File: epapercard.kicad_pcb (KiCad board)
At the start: 2 copper layers, 88.9 x 50.8 mm, 44 parts, among them P1 PROG, P2 A120699CT, Q1 2N7002KW, Q2 BSS84W, Q3 AP2305, Q4 BSS84W, Q5 2N7002KW, Q6 2N7002KW, Q7 2N7002KW, SW1 SW_PUSH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

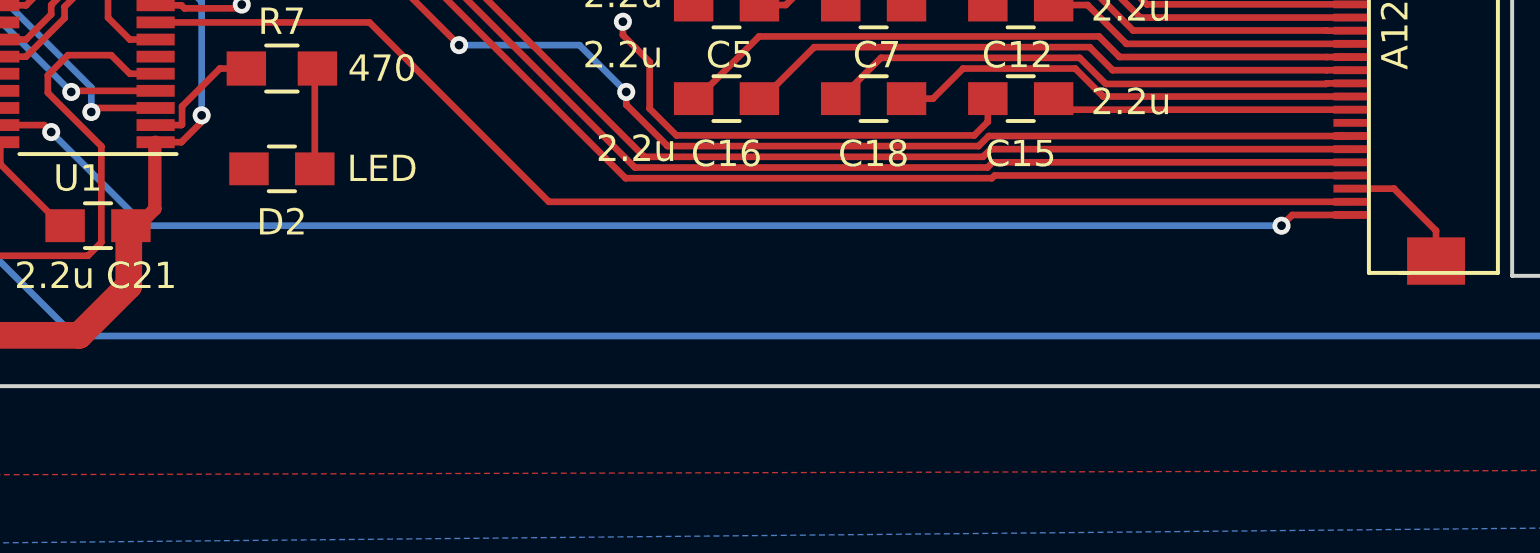
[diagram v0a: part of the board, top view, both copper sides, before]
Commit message: Updated silk
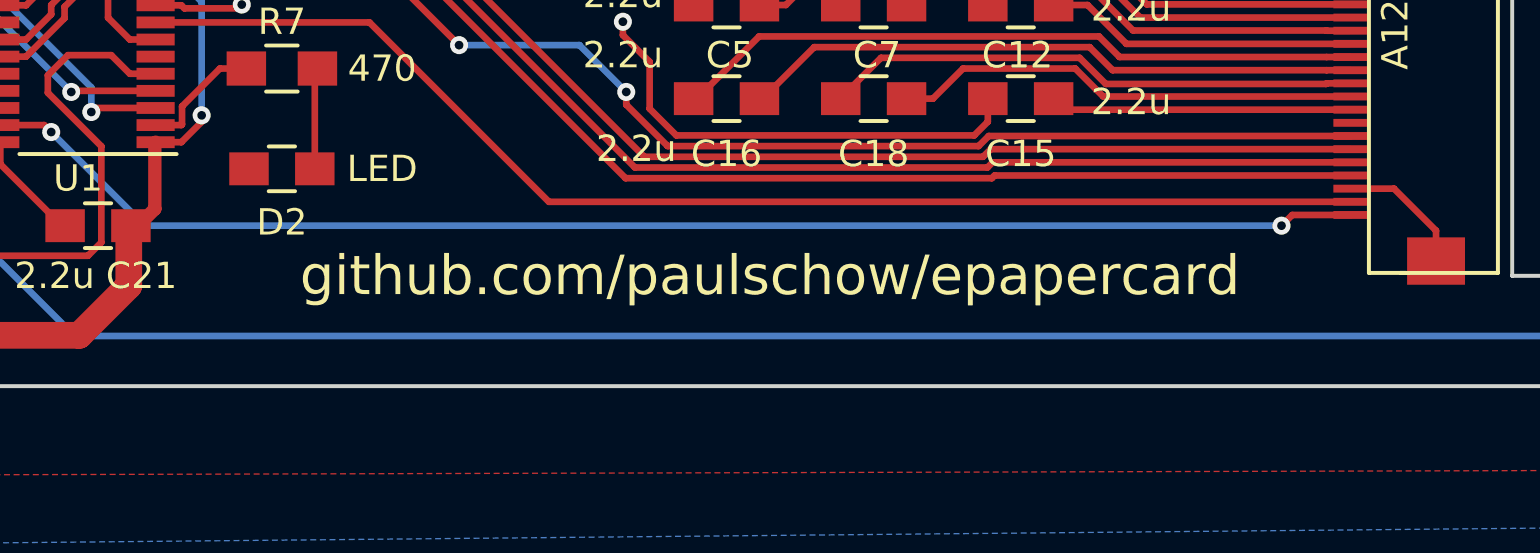
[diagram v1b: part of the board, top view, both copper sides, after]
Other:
- board text added: "github.com/paulschow/epapercard"
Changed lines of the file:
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@@
     (area 8.204287 22.759999 124.714001 86.868001)
     (thickness 1.6)
-    (drawings 29)
+    (drawings 30)
     (tracks 452)
     (zones 0)
@@
       (xy 0.317705 4.183579)) (layer B.SilkS) (width 0.01))
   )
+  (gr_text github.com/paulschow/epapercard (at 75.946 76.454) (layer F.SilkS)
+    (effects (font (size 1.5 1.5) (thickness 0.3)))
+  )
   (gr_text "Open Source\nHardware" (at 40.64 75.438) (layer B.SilkS)
     (effects (font (size 1.5 1.5) (thickness 0.3)) (justify mirror))
@@
     (effects (font (size 1.016 1.016) (thickness 0.1524)))
   )
-  (gr_text paulschow@gmail.com (at 88.138 40.386) (layer B.SilkS)
-    (effects (font (size 2.54 2.54) (thickness 0.3)) (justify mirror))
+  (gr_text paulschow@gmail.com (at 64.516 33.02) (layer B.SilkS)
+    (effects (font (size 2.54 2.54) (thickness 0.381)) (justify mirror))
   )
   (gr_text paulschow.com (at 94.996 36.322) (layer B.SilkS)
-    (effects (font (size 2.54 2.54) (thickness 0.3)) (justify mirror))
+    (effects (font (size 2.54 2.54) (thickness 0.381)) (justify mirror))
   )
   (gr_text "Paul Schow" (at 98.298 33.02) (layer B.SilkS)
-    (effects (font (size 2.54 2.54) (thickness 0.3)) (justify mirror))
+    (effects (font (size 2.54 2.54) (thickness 0.381)) (justify mirror))
   )
   (gr_text "CUT OUT" (at 105.41 63.754 90) (layer Edge.Cuts)

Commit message: Adjusting footprints
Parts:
- removed G***: LOGO, footprint:oshlogo
- P1: value PROG -> CONN_01X06
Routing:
- net BUSY: track 48.2 -> 17.8 mm
- net +3.3VP: track 74.4 -> 58.1 mm
- net GND: track 58.1 -> 42.4 mm, vias 3 -> 2
- net /RESET: track 48.3 -> 34.6 mm
- net SPI_MISO: track 57.7 -> 44.0 mm
- net SPI_MOSI: track 57.7 -> 44.1 mm
- net SPI_CLK: track 55.4 -> 41.9 mm
- net Net-(C15-Pad1): track 11.4 -> 0.59 mm
- net /VDL: track 35.7 -> 25.3 mm
- net Net-(C18-Pad1): track 17.8 -> 8.39 mm
- net Net-(C18-Pad2): track 20.4 -> 11.1 mm
- net Net-(C16-Pad1): track 23.6 -> 14.6 mm
- net Net-(C16-Pad2): track 26.3 -> 17.5 mm
- net Net-(C12-Pad1): track 11.9 -> 3.38 mm
- net Net-(C12-Pad2): track 15.5 -> 7.23 mm
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
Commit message: Basically starting over
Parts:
- C2: value 100n -> 0.1u
- Q3: value AP2305 -> BSS84W
- U1: footprint Housings_SSOP:TSSOP-20_4.4x6.5mm_Pitch0.65mm -> footprint:TSSOP-20_4.4x6.5mm_Pitch0.65mm
- moved Q4 94.4 mm to (41.3, 112.6), turned to 0 degrees
- moved R5 67.3 mm to (64.1, 112.5), turned to 0 degrees
- moved Q7 66.2 mm to (50.7, 93.8), turned to 0 degrees
- moved C4 65.8 mm to (65.2, 93.9)
- moved R3 63.5 mm to (78.4, 100.1), turned to 0 degrees
- moved C14 60.3 mm to (51.9, 115.7), turned to 0 degrees
- moved C9 59.3 mm to (47.0, 113.5), turned to 0 degrees
- moved R1 58.9 mm to (75.3, 106.3), turned to 0 degrees
- moved C11 57.5 mm to (60.3, 106.3), turned to 0 degrees
- moved D1 57.1 mm to (41.6, 107.9), turned to 0 degrees
- moved R2 55.8 mm to (69.3, 112.5), turned to 0 degrees
- moved R6 55.1 mm to (49.1, 107.3), turned to 0 degrees
- moved C17 54.5 mm to (79.3, 112.5), turned to 0 degrees
- moved Q5 52.1 mm to (42.3, 103.2), turned to 0 degrees
- moved R4 51.2 mm to (85.1, 93.9), turned to 0 degrees
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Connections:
- Q2 pad 2: Net-(C1-Pad2) -> +3V3
- Q2 pad 3: +3V3 -> Net-(C1-Pad2)
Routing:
- net +3V3: track 233.9 -> 93.9 mm, vias 4 -> 0
- net BORDER_CONTROL: track 109.9 -> 0.04 mm, vias 2 -> 0
- net /VGL: track 58.1 -> 0.00 mm
- net +3.3VP: track 58.1 -> 0.00 mm
- net /EPD_CS: track 50.3 -> 0.00 mm, vias 1 -> 0
- net SPI_MOSI: track 44.1 -> 0.00 mm
- net SPI_MISO: track 44.0 -> 0.00 mm
- net SPI_CLK: track 41.9 -> 0.00 mm
- net GND: track 42.4 -> 4.26 mm, vias 2 -> 0
- net /VDH: track 34.7 -> 0.00 mm
- net /RESET: track 34.6 -> 0.00 mm, vias 2 -> 0
- net /VGH: track 32.5 -> 0.00 mm
- net /VCOM: track 31.4 -> 0.00 mm, vias 2 -> 0
- net DISCHARGE: track 26.9 -> 0.00 mm, vias 3 -> 0
- net /VDL: track 25.3 -> 0.00 mm
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- removed copper zone on B.Cu, net GND
- removed copper zone on F.Cu, net GND
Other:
- outline, holes or cut-outs redrawn

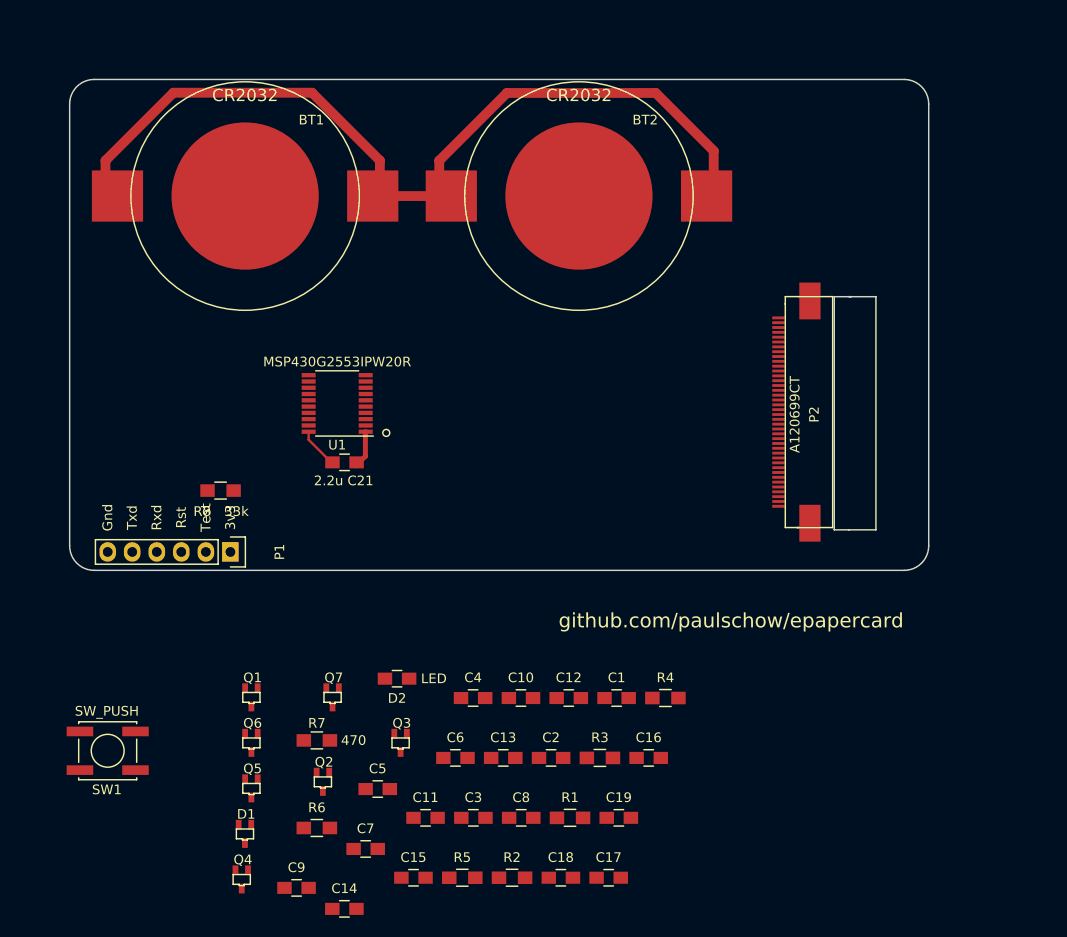
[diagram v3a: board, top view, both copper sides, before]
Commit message: Routed caps
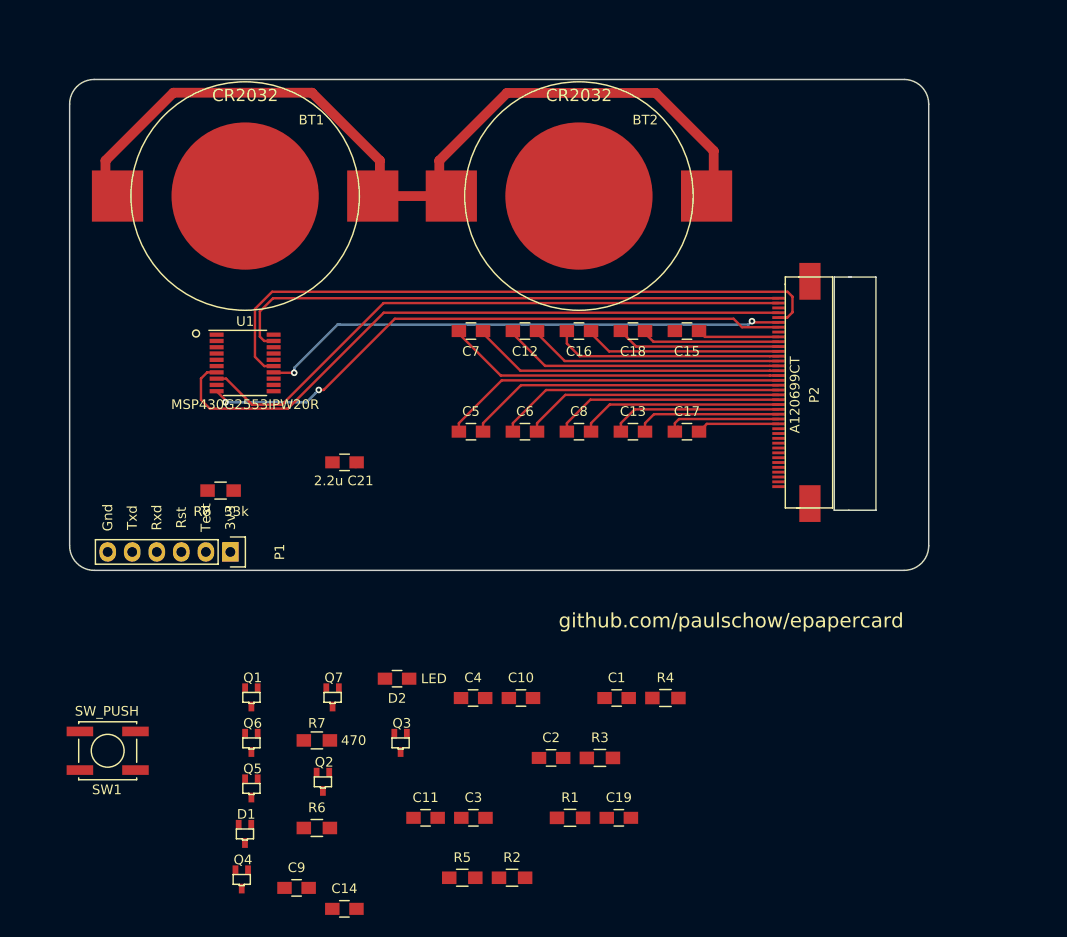
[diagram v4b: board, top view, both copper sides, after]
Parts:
- moved C15 63.3 mm to (87.4, 55.9), turned to 180 degrees
- moved C18 57.1 mm to (81.8, 55.9), turned to 180 degrees
- moved C7 54.7 mm to (65.0, 55.9), turned to 180 degrees
- moved C17 46.9 mm to (87.4, 66.3)
- moved C16 44.8 mm to (76.2, 55.9), turned to 180 degrees
- moved C8 40.4 mm to (76.2, 66.3)
- moved C12 38.2 mm to (70.6, 55.9), turned to 180 degrees
- moved C5 38.2 mm to (65.0, 66.3)
- moved C13 36.3 mm to (81.8, 66.3)
- moved C6 34.5 mm to (70.6, 66.3)
- moved U1 10.4 mm to (41.7, 59.2), turned to 0 degrees
- moved P2 2.03 mm to (101.9, 62.5)
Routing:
- net SPI_CLK: track 0.00 -> 68.3 mm
- net SPI_MOSI: track 0.00 -> 67.1 mm
- net BUSY: track 0.00 -> 63.6 mm
- net /RESET: track 0.00 -> 62.7 mm, vias 0 -> 2
- net /EPD_CS: track 0.00 -> 58.5 mm
- net SPI_MISO: track 0.00 -> 54.8 mm, vias 0 -> 2
- net Net-(C5-Pad1): track 0.00 -> 35.8 mm
- net Net-(C7-Pad2): track 0.00 -> 35.1 mm
- net Net-(C5-Pad2): track 0.00 -> 33.1 mm
- net Net-(C7-Pad1): track 0.00 -> 32.4 mm
- net Net-(C6-Pad1): track 0.00 -> 29.8 mm
- net Net-(C12-Pad2): track 0.00 -> 29.1 mm
- net Net-(C6-Pad2): track 0.00 -> 27.1 mm
- net Net-(C12-Pad1): track 0.00 -> 26.4 mm
- net Net-(C8-Pad1): track 0.00 -> 23.9 mm
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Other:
- outline, holes or cut-outs redrawn

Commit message: Placed all components
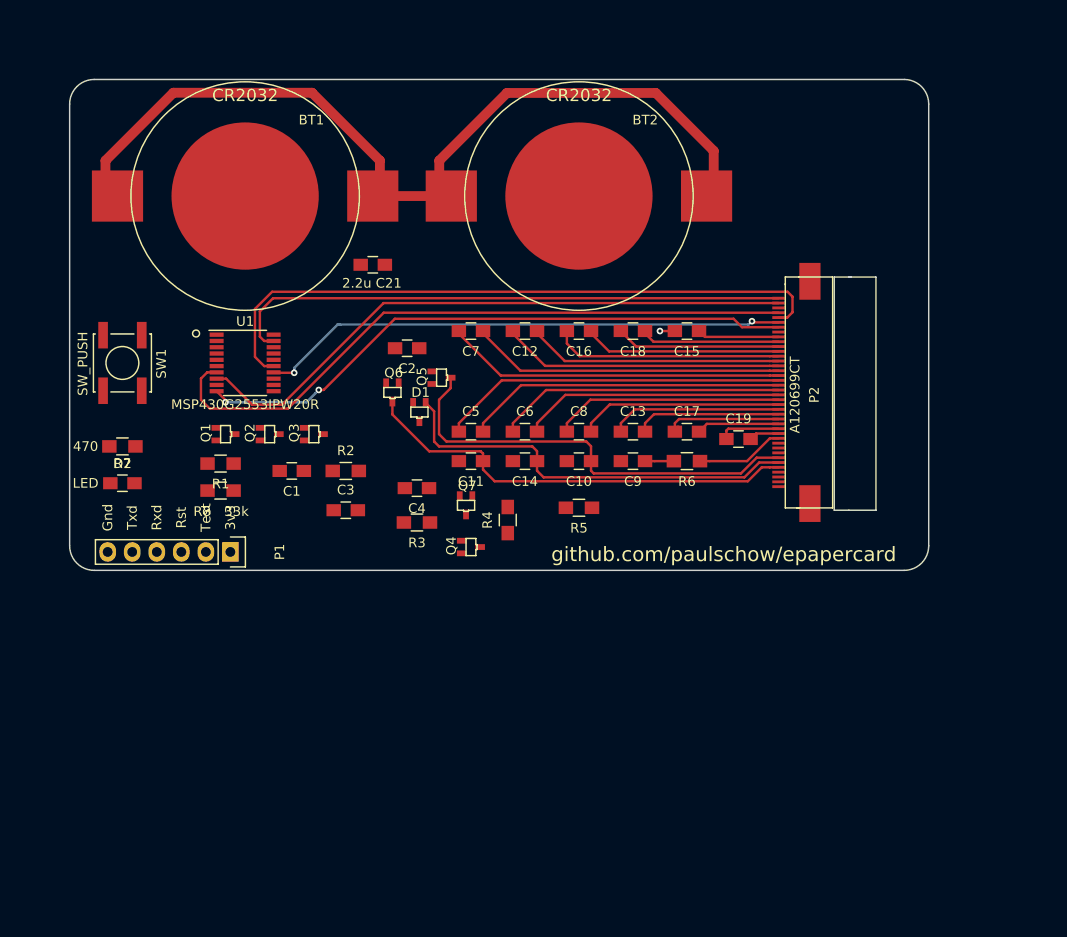
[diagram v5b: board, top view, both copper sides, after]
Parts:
- moved C9 56.2 mm to (81.8, 69.3), turned to 180 degrees
- moved R6 53.9 mm to (87.4, 69.3), turned to 180 degrees
- moved R1 51.5 mm to (39.1, 69.6), turned to 180 degrees
- moved C14 50.0 mm to (70.6, 69.3), turned to 180 degrees
- moved D1 47.2 mm to (59.7, 64.3)
- moved Q5 46.8 mm to (62.0, 60.7), turned to 90 degrees
- moved R2 45.5 mm to (52.1, 70.4)
- moved C2 44.9 mm to (58.4, 57.7), turned to 180 degrees
- moved Q4 41.8 mm to (65.0, 78.2), turned to 90 degrees
- moved C19 41.1 mm to (92.7, 67.1)
- moved C1 41.0 mm to (46.5, 70.4), turned to 180 degrees
- moved SW1 40.2 mm to (29.0, 59.2), turned to 270 degrees
- moved R5 40.1 mm to (76.2, 74.2), turned to 180 degrees
- moved Q6 39.1 mm to (56.9, 62.2)
- moved C11 37.2 mm to (65.0, 69.3), turned to 180 degrees
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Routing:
- net /VDH: track 0.00 -> 45.7 mm
- net /VGH: track 0.00 -> 45.3 mm
- net /VGL: track 0.00 -> 43.4 mm
- net Net-(P2-Pad30): track 0.00 -> 9.10 mm
- net Net-(C19-Pad1): track 0.00 -> 6.35 mm
- net Net-(C19-Pad2): track 0.00 -> 3.13 mm
- net /VCOM: track 0.00 -> 2.99 mm
- net GND: track 0.12 -> 1.54 mm, vias 0 -> 1
- net +3V3: track 90.4 -> 89.8 mm

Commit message: All routed
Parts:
- moved C21 26.7 mm to (46.5, 74.4), turned to 180 degrees
- moved D2 23.9 mm to (51.8, 64.5), turned to 0 degrees
- moved R7 23.7 mm to (51.8, 61.7), turned to 180 degrees
- turned U1 to 180 degrees
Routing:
- net +3V3: track 89.8 -> 161.9 mm
- net +3.3VP: track 0.00 -> 67.6 mm
- net GND: track 1.54 -> 65.1 mm, vias 1 -> 14
- net /VDL: track 0.00 -> 42.3 mm
- net BORDER_CONTROL: track 0.00 -> 39.6 mm, vias 0 -> 2
- net DISCHARGE: track 0.00 -> 36.6 mm, vias 0 -> 2
- net /BORDER: track 0.00 -> 34.6 mm
- net /VCOM: track 2.99 -> 36.0 mm, vias 0 -> 2
- net /rxd: track 0.00 -> 28.8 mm, vias 0 -> 1
- net /button: track 0.00 -> 28.5 mm, vias 0 -> 2
- net PANEL_ON: track 0.00 -> 26.4 mm, vias 0 -> 2
- net /rst: track 0.00 -> 25.3 mm, vias 0 -> 2
- net /txd: track 0.00 -> 25.0 mm, vias 0 -> 1
- net /test: track 0.00 -> 23.8 mm, vias 0 -> 1
- net SPI_CLK: track 68.3 -> 54.0 mm
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- added copper zone on B.Cu, net GND
- added copper zone on F.Cu, net GND

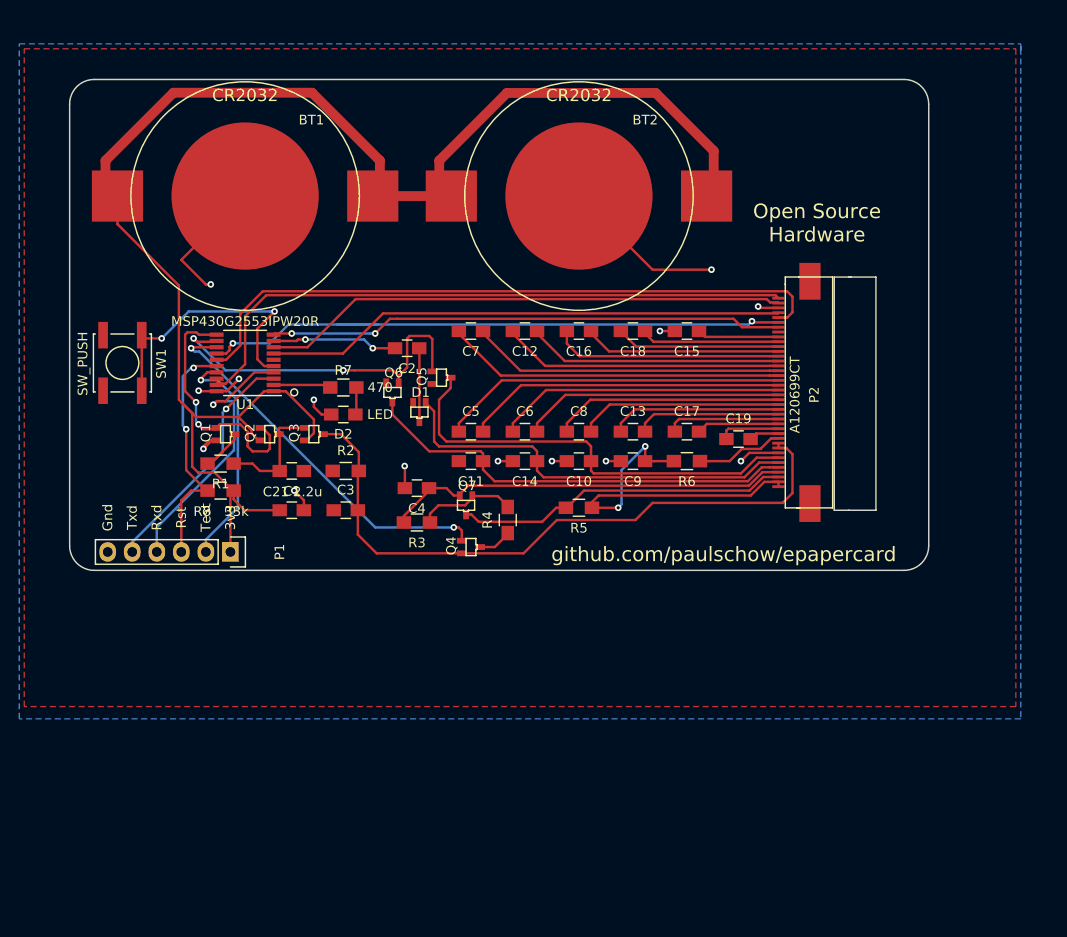
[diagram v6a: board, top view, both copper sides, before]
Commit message: Fixed silk
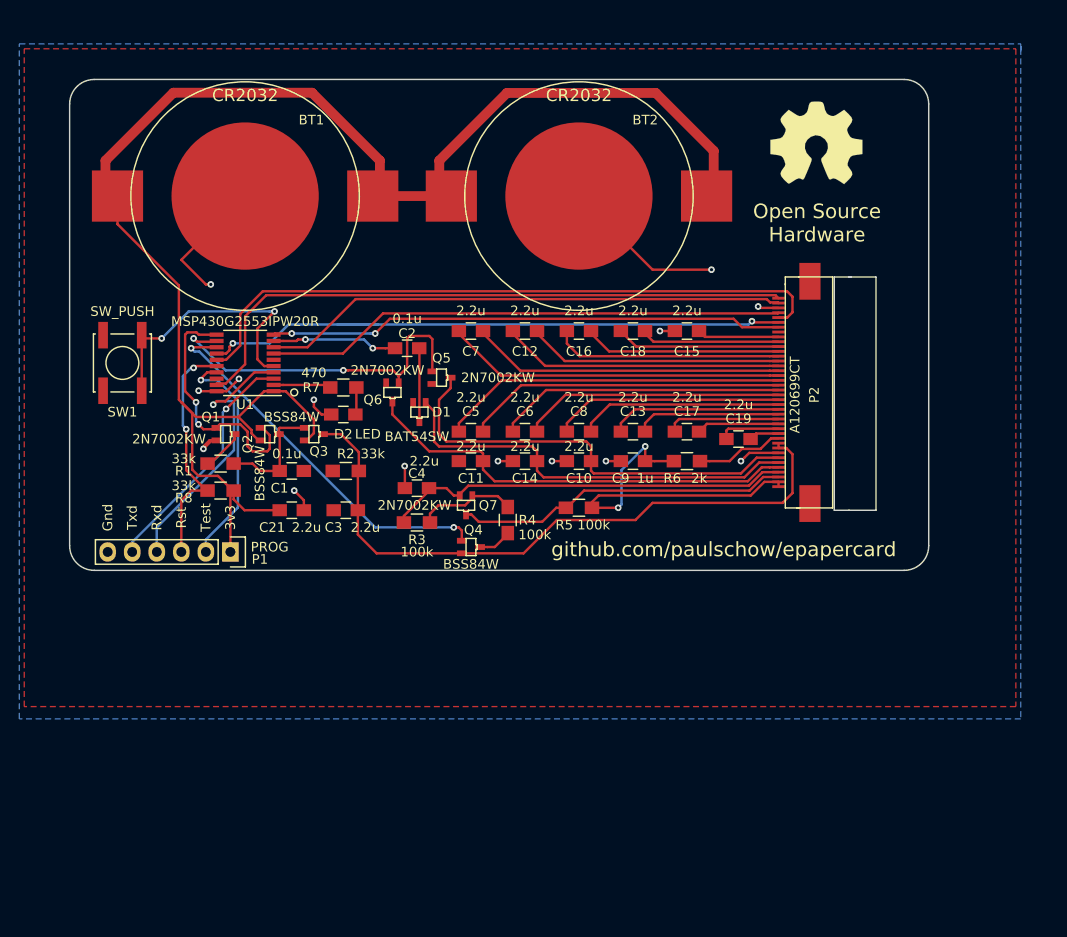
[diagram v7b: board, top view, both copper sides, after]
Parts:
- added G***: LOGO, footprint:oshlogo, F.Cu at (100.8, 36.3)
- P1: value CONN_01X06 -> PROG
